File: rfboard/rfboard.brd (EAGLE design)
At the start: 30 x 60 mm, 18 parts, among them U1 MAX1555

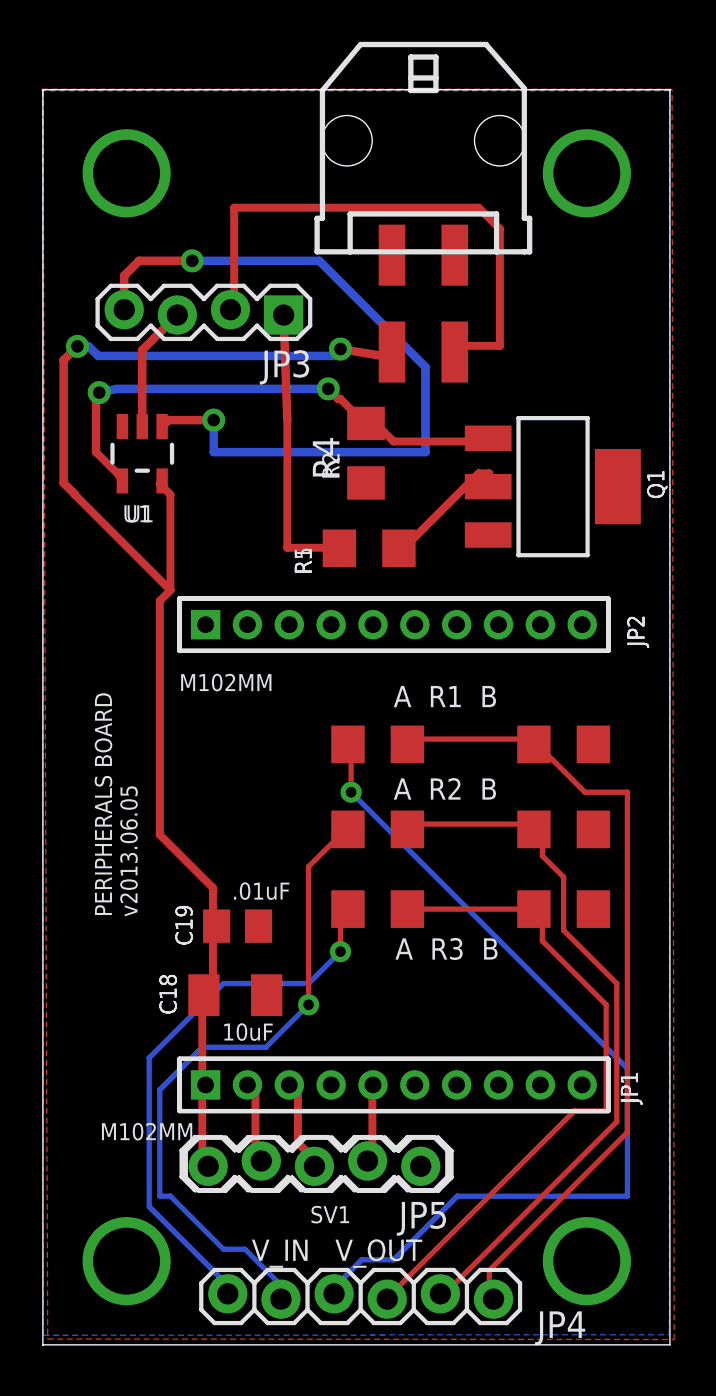
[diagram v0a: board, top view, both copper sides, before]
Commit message: added ambient light sensor and 3 voltage dividers, new XBEE connection
-added the MONOLITHIC PHOTODIODE AND SINGLE-SUPPLY TRANSIMPEDANCE AMPLIFIER, ie OPT101 abmient light sensors
-added circuitry for the OPT101
-added header pin, labeled AMB_OUT, for the output of the OPT101
-added three extra voltage dividers for future DMS sensors
-added six 2mm 2pin headers for the DMS Sensors cables
--NOTE: the DMS sensor headers are currently GND, VCC, DATA from left to right
-changed XBEE connection to one 2mm 10pin header for new adaptor board
-change circuitry for proper connections
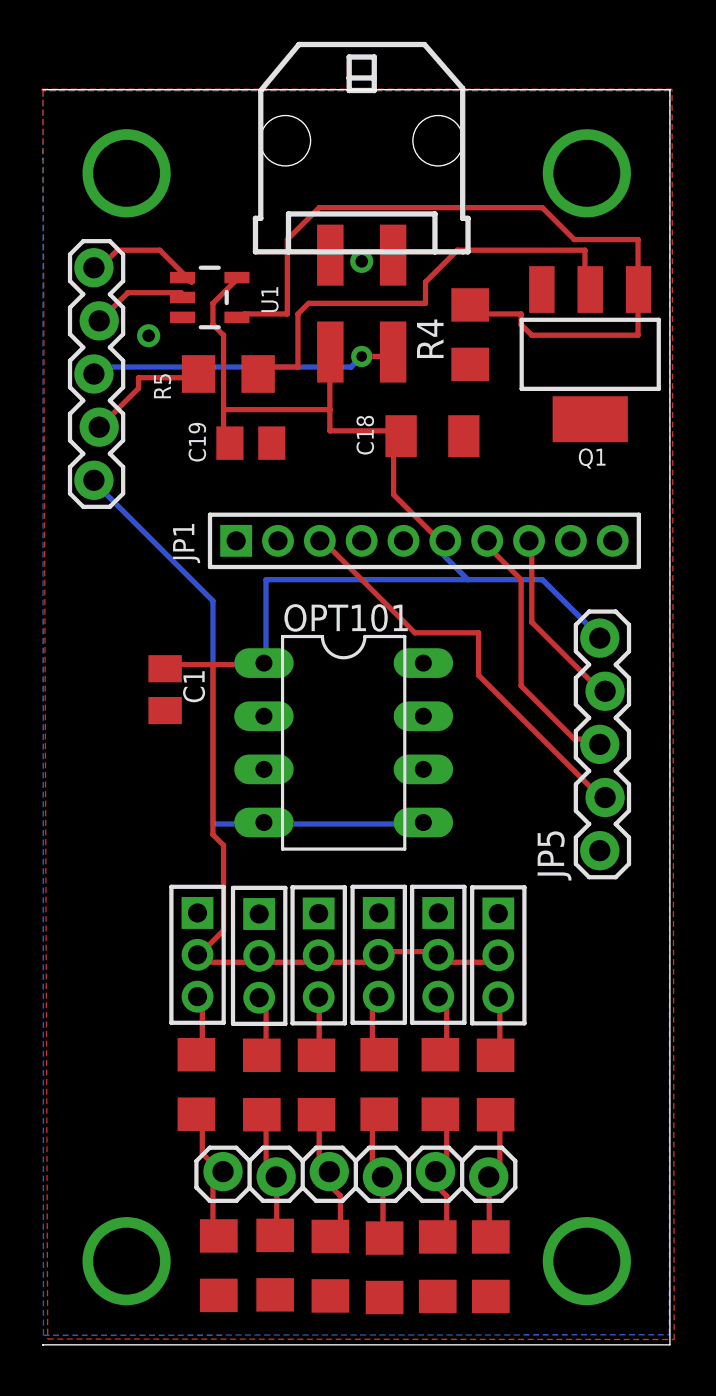
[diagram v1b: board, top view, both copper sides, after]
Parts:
- removed JP3: (no value), SparkFun-Connectors:1X04_LOCK
- added C1: .01uF, rcl:C0805K
- added JP10, JP11, JP6, JP7, JP8, JP9: (no value), pinhead-2:1X03M
- added OPT101: (no value), ic-package:DIL08
- added R4A, R4B, R5A, R5B, R6A, R6B: (no value), rcl:R1206
- JP1: value M102MM -> (none); device SparkFun-Connectors 2:1X10-2MM -> pinhead-2:1X10M
- JP2: value M102MM -> (none); device SparkFun-Connectors 2:1X10-2MM -> SparkFun-Connectors:1X05_LOCK
- moved C18 28.3 mm to (18.6, 43.4)
- moved JP1 28.0 mm to (18.2, 38.4)
- moved R1B 25.2 mm to (21.4, 3.73), turned to 90 degrees
- moved C19 23.1 mm to (9.94, 43.1)
- moved R2B 21.8 mm to (18.9, 3.73), turned to 90 degrees
- moved R3B 19.2 mm to (16.3, 3.68), turned to 90 degrees
- moved JP5 17.3 mm to (26.7, 23.6), turned to 90 degrees
- moved R1A 17.2 mm to (21.6, 12.4), turned to 90 degrees
- moved R2A 12.6 mm to (19.0, 12.4), turned to 90 degrees
- moved R5 10.7 mm to (8.86, 46.4)
- moved JP2 8.65 mm to (2.57, 41.3), turned to 90 degrees
- moved R3A 8.38 mm to (16.1, 12.4), turned to 90 degrees
- moved U1 8.13 mm to (7.98, 50.1), turned to 270 degrees
- moved R4 7.54 mm to (20.4, 48.3)
- moved Q1 6.57 mm to (26.2, 47.3), turned to 180 degrees
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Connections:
- removed net V_1: JP4.4, R1A.2
- removed net V_2: JP4.5, R2A.2
- removed net V_3: JP4.6, R3A.2
- new net AMB_OUT: JP2.1, OPT101.4, OPT101.5
- new net DATA1: JP6.3, R1A.2
- new net DATA2: JP8.3, R2A.2
- new net DATA3: JP11.3, R3A.2
- new net DATA4: JP7.3, R4A.2
- new net DATA5: JP9.3, R5A.2
- new net DATA6: JP10.3, R6A.2
- new net VD4: JP4.4, R4A.1, R4B.2
- new net VD5: JP4.5, R5A.1, R5B.2
- new net VD6: JP4.6, R6A.1, R6B.2
- net DIN: now also JP1.7; no longer JP1.3
- net DOUT: now also JP1.8; no longer JP1.2
- net GND: now also C1.2, JP1.4, JP10.1, JP11.1, JP6.1, JP7.1, JP8.1, JP9.1, OPT101.3, OPT101.8, R4B.1, R5B.1, R6B.1; no longer JP1.10
- net LED5V: now also JP2.3; no longer JP3.2
- net LEDRETURN: now also JP2.2; no longer JP3.1
- net PWM_IN: now also JP2.4; no longer JP3.3
- net RESET: now also JP1.3; no longer JP1.5
- net UART_IN: now also JP2.5; no longer JP3.4
- net VCC: now also C1.1, JP1.6, JP10.2, JP11.2, JP6.2, JP7.2, JP8.2, JP9.2, OPT101.1; no longer JP1.1
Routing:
- net V_1: track 43.4 -> 0.00 mm, vias 1 -> 0
- net VD1: track 38.8 -> 6.12 mm
- net V_2: track 31.5 -> 0.00 mm, vias 1 -> 0
- net UART_IN: track 36.7 -> 6.31 mm, vias 2 -> 0
- net AMB_OUT: track 0.00 -> 28.9 mm
- net VD2: track 33.8 -> 6.73 mm
- net V_3: track 26.8 -> 0.00 mm, vias 1 -> 0
- net VD3: track 31.6 -> 6.45 mm
- net VCC: track 64.7 -> 86.5 mm, vias 2 -> 0
- net RESET: track 3.70 -> 19.8 mm
- net N$5: track 6.44 -> 22.1 mm
- net N$3: track 24.5 -> 37.5 mm, vias 2 -> 0
- net LED5V: track 26.0 -> 14.8 mm, vias 0 -> 1
- net DIN: track 4.54 -> 12.5 mm
- net LEDRETURN: track 13.6 -> 6.06 mm
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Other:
- board text removed: ".01uF"
- board text removed: "10uF"
- board text removed: "A R1 B"
- board text removed: "A R2 B"
- board text removed: "A R3 B"
- board text removed: "C18"
- board text removed: "C19"
- board text removed: "JP1"
- board text removed: "JP2"
- board text removed: "M102MM"
- board text removed: "PERIPHERALS BOARD v2013.06.05"
- board text removed: "Q1"
- board text removed: "R1"
- board text removed: "R2"
- board text removed: "SV1"
- board text removed: "U1"
- board text removed: "V_IN V_OUT"

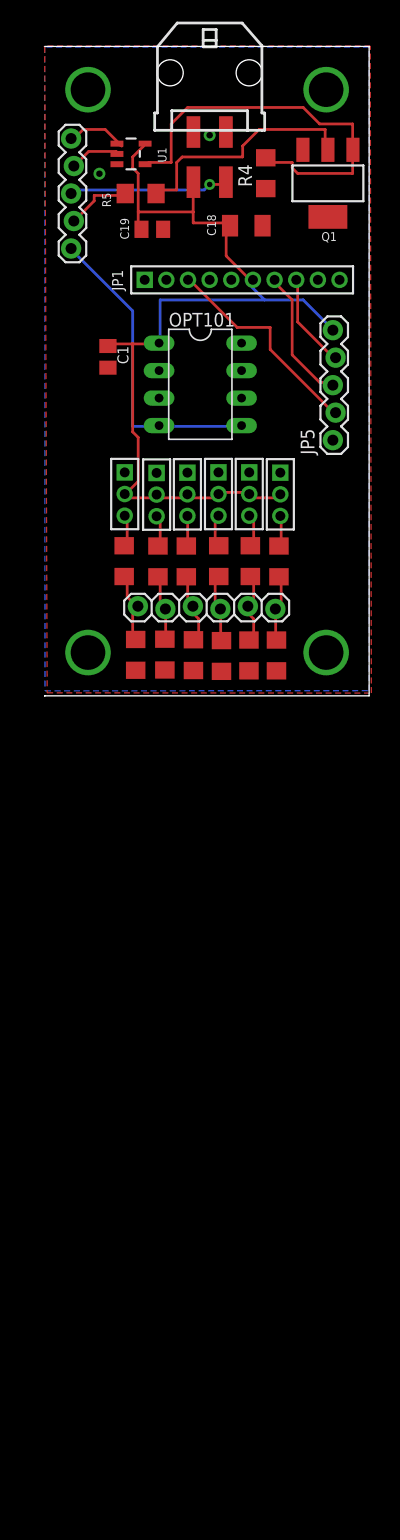
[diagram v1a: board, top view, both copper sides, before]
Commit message: changing XBee pinout, and adding logic converters
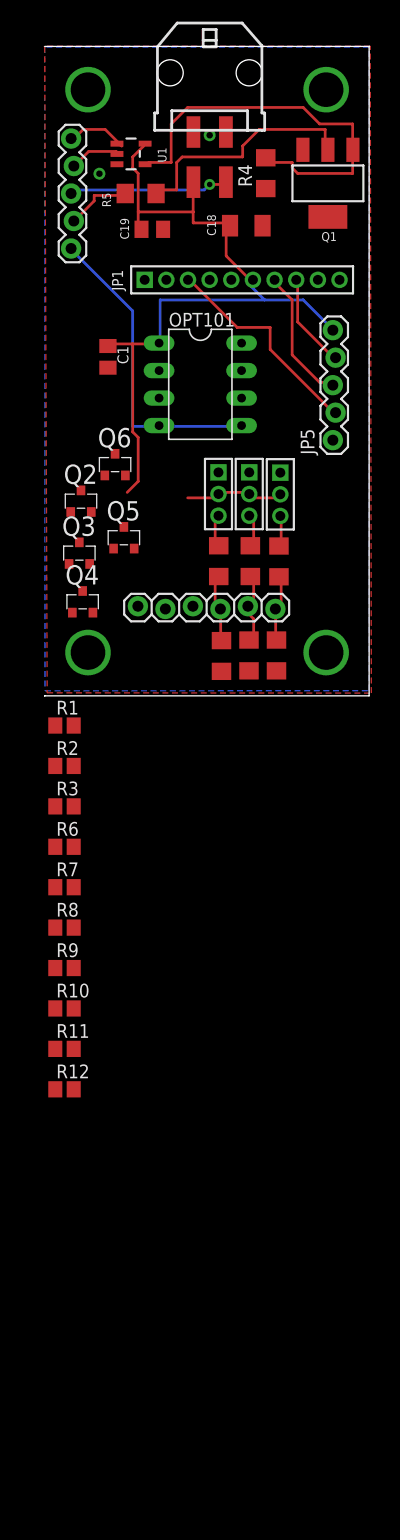
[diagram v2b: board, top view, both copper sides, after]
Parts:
- removed JP10, JP7, JP9: (no value), pinhead-2:1X03M
- removed R4A, R4B, R5A, R5B, R6A, R6B: (no value), rcl:R1206
- added Q2, Q3, Q4, Q5, Q6: IRLML5203, ngohara_parts:MICRO3
- added R1, R10, R11, R12, R2, R3, R6, R7, R8, R9: (no value), resistor:R0805
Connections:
- removed net DATA4: JP7.3, R4A.2
- removed net DATA5: JP9.3, R5A.2
- removed net DATA6: JP10.3, R6A.2
- removed net LED5V: JP2.3, X2.P$4
- removed net VCC: C1.1, C18.1, C19.1, JP1.6, JP10.2, JP11.2, JP5.5, JP6.2, JP7.2, JP8.2, JP9.2, OPT101.1, U1.5, X2.P$3
- removed net VD4: JP4.4, R4A.1, R4B.2
- removed net VD5: JP4.5, R5A.1, R5B.2
- removed net VD6: JP4.6, R6A.1, R6B.2
- new net 3.3V: C1.1, C18.1, C19.1, JP11.2, JP6.2, JP8.2, OPT101.1, U1.5, X2.P$3
- new net 5V: JP2.3, R1.1, R11.1, R3.1, R7.1, R9.1
- new net N$1: Q4.2, R3.2
- new net N$10: Q5.3, R8.2
- new net N$11: Q6.3, R12.2
- new net N$12: Q6.2, R11.2
- new net N$18: X2.P$4
- new net N$2: Q4.3, R6.2
- new net N$4: Q3.3, R2.2
- new net N$6: Q3.2, R1.2
- new net N$7: Q2.2, R9.2
- new net N$8: Q2.3, R10.2
- new net N$9: Q5.2, R7.2
- net GND: now also Q2.1, Q3.1, Q4.1, Q5.1, Q6.1, R10.1, R12.1, R2.1, R6.1, R8.1; no longer JP1.4, JP10.1, JP5.1, JP7.1, JP9.1, R4B.1, R5B.1, R6B.1
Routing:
- net VCC: track 86.5 -> 0.00 mm
- net 3.3V: track 0.00 -> 77.2 mm
- net LED5V: track 14.8 -> 0.00 mm, vias 1 -> 0
- net 5V: track 0.00 -> 14.3 mm, vias 0 -> 1
- net VD6: track 6.81 -> 0.00 mm
- net VD4: track 6.52 -> 0.00 mm
- net VD5: track 6.22 -> 0.00 mm
- net DATA5: track 2.94 -> 0.00 mm
- net DATA6: track 2.93 -> 0.00 mm
- net DATA4: track 2.80 -> 0.00 mm

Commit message: changing logic converters and pinout
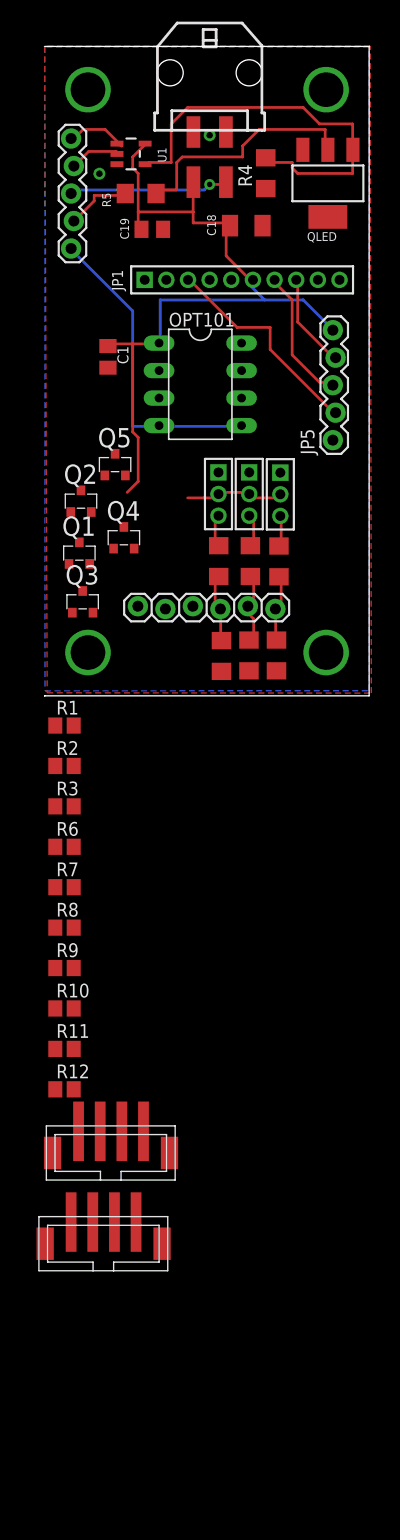
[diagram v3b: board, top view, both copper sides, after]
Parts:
- removed Q6: IRLML5203, ngohara_parts:MICRO3
- added 3.3V, 5V: JST-PH4-SMD, jst-ph:JST-PH4-SMD
- added QLED: (no value), SparkFun-DiscreteSemi:SOT223
- Q1: value (none) -> IRLML5203; device SparkFun-DiscreteSemi:SOT223 -> ngohara_parts:MICRO3
- moved Q1 41.2 mm to (3.20, 13.2), turned to 0 degrees
- moved Q4 7.04 mm to (7.32, 14.6)
- moved Q5 6.81 mm to (6.50, 21.4)
- moved Q3 4.51 mm to (3.51, 8.69)
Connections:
- removed net N$1: Q4.2, R3.2
- removed net N$10: Q5.3, R8.2
- removed net N$2: Q4.3, R6.2
- removed net N$4: Q3.3, R2.2
- removed net N$6: Q3.2, R1.2
- removed net N$7: Q2.2, R9.2
- removed net N$8: Q2.3, R10.2
- removed net N$9: Q5.2, R7.2
- new net H1: 5V.P$1, Q1.2, R1.2
- new net H2: 5V.P$2, Q2.2, R9.2
- new net H3: 5V.P$3, Q3.2, R3.2
- new net H4: 5V.P$4, Q4.2, R7.2
- new net L1: 3.3V.P$1, Q1.3, R2.2
- new net L2: 3.3V.P$2, Q2.3, R10.2
- new net L3: 3.3V.P$3, Q3.3, R6.2
- new net L4: 3.3V.P$4, Q4.3, R8.2
- new net N$13: R11.1
- new net N$14: Q5.1, R12.1
- net 5V: no longer R11.1
- net GND: now also Q1.1, QLED.3; no longer Q1.3, Q5.1, Q6.1, R12.1
- net N$11: now also Q5.3; no longer Q6.3
- net N$12: now also Q5.2; no longer Q6.2
- net N$3: now also QLED.1; no longer Q1.1
- net N$5: now also QLED.2; no longer Q1.2

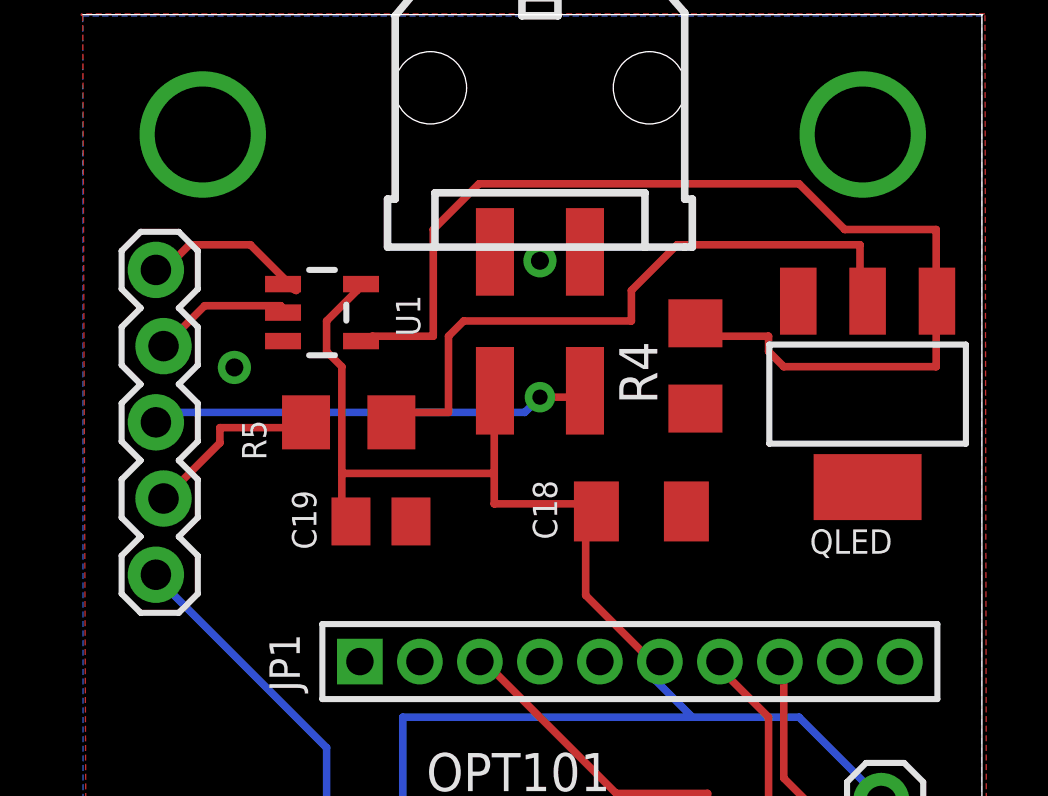
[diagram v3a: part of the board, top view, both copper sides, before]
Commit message: deleted AND circuit from RF board
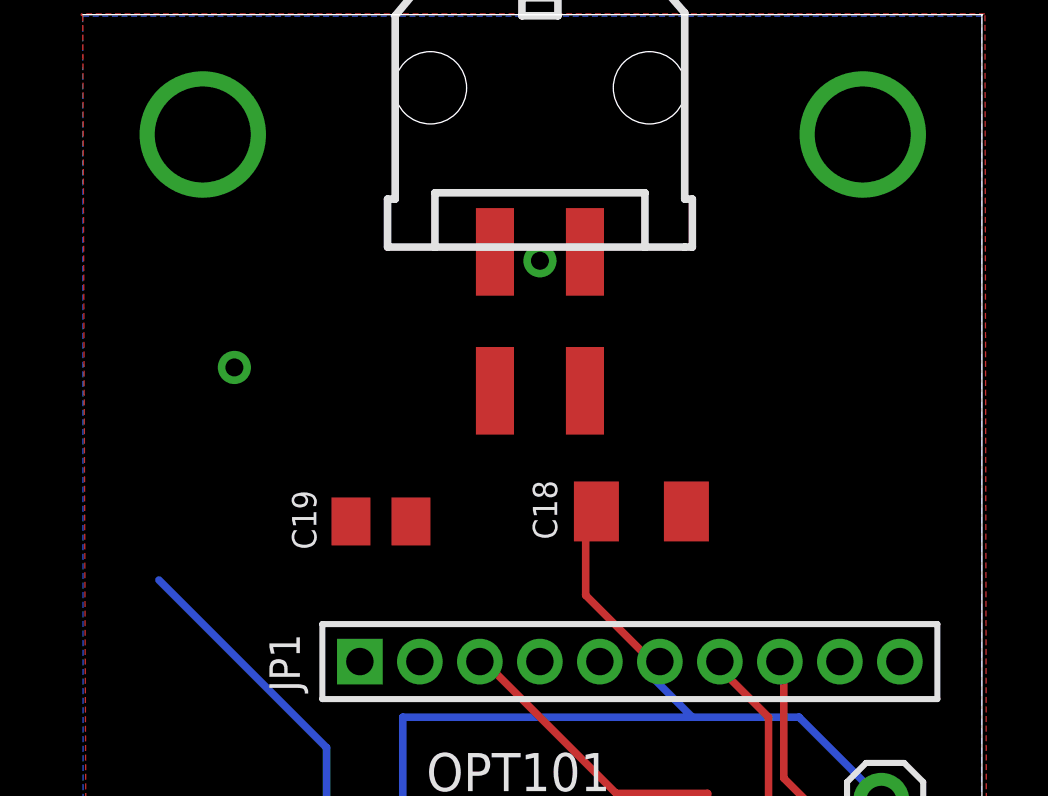
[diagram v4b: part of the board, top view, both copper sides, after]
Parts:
- removed JP2: (no value), SparkFun-Connectors:1X05_LOCK
- removed QLED: (no value), SparkFun-DiscreteSemi:SOT223
- removed R4, R5: (no value), rcl:R1206
- removed U1: MAX1555, SparkFun-PowerIC:SOT23-5
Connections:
- removed net LEDRETURN: JP2.2, R5.2
- removed net N$18: X2.P$4
- removed net N$3: QLED.1, R4.2, U1.4
- removed net N$5: QLED.2, R5.1
- removed net PWM_IN: JP2.4, U1.2
- removed net UART_IN: JP2.5, U1.1
- net 3.3V: no longer U1.5
- net 5V: now also X2.P$4; no longer JP2.3
- net AMB_OUT: no longer JP2.1
- net GND: no longer QLED.3, R4.1, U1.3
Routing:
- net N$3: track 37.5 -> 0.00 mm
- net N$5: track 22.1 -> 0.00 mm
- net 3.3V: track 77.2 -> 57.1 mm
- net 5V: track 14.3 -> 0.00 mm, vias 1 -> 0
- net UART_IN: track 6.31 -> 0.00 mm
- net LEDRETURN: track 6.06 -> 0.00 mm
- net PWM_IN: track 4.70 -> 0.00 mm
